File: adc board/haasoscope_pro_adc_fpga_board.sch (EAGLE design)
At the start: 562 parts, among them CN2 12Vin, IC1 ADC12DL2500ACF, IC13 LMH5401IRMST, IC14 LMH6401IRMZR, IC15 SN74AVC4T774PWR, IC17 DAC8562SDGSR, IC18 TLV9102IPWR, IC2 SN74AVC4T774PWR, IC21 LMH5401IRMST, IC22 TPS7A7200RGTR, IC23 TPS7A7200RGTR, IC24 TPS7A7200RGTR, IC25 TPS72325DBVR, IC26 TPS7A7200RGTR, IC27 TPS7A7200RGTR, IC28 TPS7A7200RGTR, IC29 LMH6401IRMZR, IC3 ADC122S021CIMM_NOPB, IC30 SN74AVC4T774PWR, IC33 TLV9102IPWR, IC4 TLV9102IPWR, IC5 EP4CE30F23C6N, IC6 EPCQ16ASI8N, IC8 FT232HQ, IC9 93LC56B, J1 2p-2.54, J10 8pin, J11 8pin, J13 8pin, J14 2x5, J15 test1, J2 test1, J30 2p-2.54, J31 2p-2.54, J32 2p-2.54, J33 2p-2.54, J34 2p-2.54, J35 2p-2.54, J36 2p-2.54, J37 2p-2.54, J39 2p-2.54, J40 2p-2.54, J41 2p-2.54, J42 2p-2.54, J43 2p-2.54, J44 2p-2.54, J45 2p-2.54, J46 2p-2.54, J8 8pin, K10 G6K-2F-RF-DC3, K11 G6K-2F-RF-DC3, K12 G6K-2F-RF-DC3, K5 AQY21SOP, K6 G6K-2F-RF-DC3, K7 G6K-2F-RF-DC3, K9 AQY21SOP, Q1 S8050, Q4 S8050, Q5 S8050, Q7 S8050, Q8 S8050, Q9 S8050, SW3 SKQGADE010, SW4 SKQGADE010, U2 ADF4350BCPZ, U6 AMS1117-1.2, X1 USBC, Y2 OSCILLATORSMD-5X3, Y3 12MHz

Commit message: make 2v5+ from 3v3 instead of 2v8+, make 1v2 from 1v5d using standard TPS7A7200RGTR instead of 3v3 with ams117-1.2
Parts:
- removed C76, C80: 10uF, Nordic_nRF:CAPACITOR_0805_N
- removed C77, C81: 0.1uF, Nordic_nRF:CAPACITOR_0402_N
- removed U6: AMS1117-1.2, MF_IC_Power:NCP1117LPST33T3G
- added C52: 10uF, Nordic_nRF:CAPACITOR_0805_N
- added C53, C54, C73: 0.1uF, Nordic_nRF:CAPACITOR_0402_N
- added IC7: TPS7A7200RGTR, TPS7A7200RGTR:TPS7A7200RGTR
- added J3: 2p-2.54, Seeed-Connector:DIP-BLACK-MALE-HEADER-VERT(2P-2.54)
- added R137: 100k, FlashPCB_Resistors:RES-0402
- added R161: 10k, FlashPCB_Resistors:RES-0402
- R230: value 56k -> 100k
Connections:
- removed net 2V8+: C278.1, C298.1, C299.1, C300.1, C301.1, IC26.EN, IC26.IN_1, IC26.IN_2, J43.1, L12.2, R229.P$2
- new net 1V5D: C278.1, C298.1, C299.1, C300.1, C301.1, C54.1, IC7.EN, IC7.IN_1, IC7.IN_2, J43.1, L12.2, R229.P$2
- new net N$23: R137.P$2, R230.P$1
- new net PG1V2: IC7.PG, R161.P$2
- net 1V2: now also C52.1, C53.1, IC7.OUT_1, IC7.OUT_2, IC7.SNS, J3.2, R161.P$1; no longer C76.2, C77.2, U6.VOUT
- net 3V3: now also C73.1, IC26.EN, IC26.IN_1, IC26.IN_2; no longer C80.2, C81.2, U6.VIN
- net GND: now also C52.2, C53.2, C54.2, C73.2, IC7.100MV, IC7.200MV, IC7.400MV, IC7.EP, IC7.GND, J3.1, R137.P$1; no longer C76.1, C77.1, C80.1, C81.1, R230.P$1, U6.GND/ADJ
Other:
- note added: "1V2 for FPGA"
- note added: "ADC power filters"
- note added: "FPGA power filters"
- note added: "For 2V5+, take input from 3V3 Only ~300mA needed"
- note added: "Rbot = Rtop/(Vout-1) =100k/(1.5-1) = 200k"
- note added: "V+ for FPGA reg ~ 1.5V"
- note removed: "Rbot = Rtop/(Vout-1) =100k/(1.5-1) = ~200k"
- note removed: "V+ for input amp reg ~ 2.8V"
- moved on the sheet: C253, C254, C275, C276, C277, C278, C298, C299, C300, C301, C34, C40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

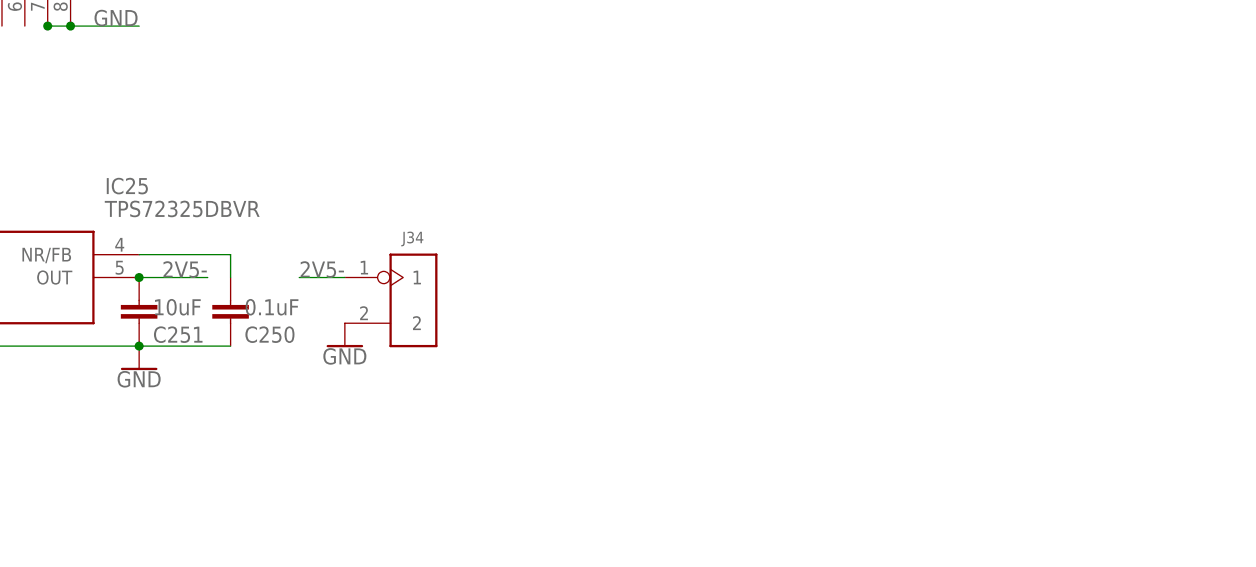
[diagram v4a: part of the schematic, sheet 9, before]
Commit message: Use 2 -2.5V regulators, one for input A, another for input B, since we need more than 200mA
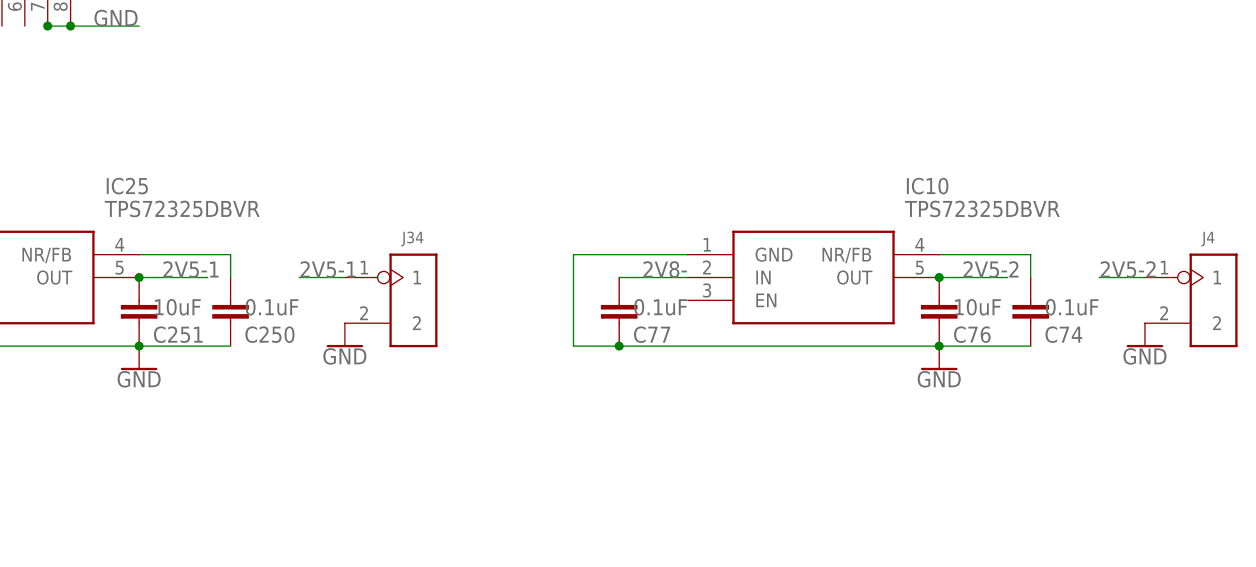
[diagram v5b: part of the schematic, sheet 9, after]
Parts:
- added C74, C77: 0.1uF, Nordic_nRF:CAPACITOR_0402_N
- added C76: 10uF, Nordic_nRF:CAPACITOR_0805_N
- added IC10: TPS72325DBVR, TPS72325DBVR:TPS72325DBVR
- added J4: 2p-2.54, Seeed-Connector:DIP-BLACK-MALE-HEADER-VERT(2P-2.54)
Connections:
- removed net 2V5-: C108.P$1, C110.P$1, C112.P$1, C129.P$1, C133.P$1, C135.P$1, C251.1, C56.P$1, C78.P$1, C85.P$1, C87.P$1, C89.P$1, C91.P$1, C95.P$1, C97.P$1, FL1.THERMAL, FL1.VS-, FL2.THERMAL, FL2.VS-, FL3.THERMAL, FL3.VS-, FL4.THERMAL, FL4.VS-, IC13.VS-_1, IC13.VS-_2, IC14.VS-_1, IC14.VS-_2, IC18.V-, IC21.VS-_1, IC21.VS-_2, IC25.OUT, IC29.VS-_1, IC29.VS-_2, IC33.V-, J34.1
- new net 2V5-1: C251.1, C78.P$1, C85.P$1, C87.P$1, C89.P$1, C91.P$1, C95.P$1, C97.P$1, FL1.THERMAL, FL1.VS-, FL3.THERMAL, FL3.VS-, IC13.VS-_1, IC13.VS-_2, IC14.VS-_1, IC14.VS-_2, IC18.V-, IC25.OUT, J34.1
- new net 2V5-2: C108.P$1, C110.P$1, C112.P$1, C129.P$1, C133.P$1, C135.P$1, C56.P$1, C76.1, FL2.THERMAL, FL2.VS-, FL4.THERMAL, FL4.VS-, IC10.OUT, IC21.VS-_1, IC21.VS-_2, IC29.VS-_1, IC29.VS-_2, IC33.V-, J4.1
- new net N$61: C74.1, IC10.NR/FB
- net 2V8-: now also C77.1, IC10.IN
- net GND: now also C74.2, C76.2, C77.2, IC10.GND, J4.2
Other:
- note added: "2A max current 180mV dropout at 2A"
- note added: "2V5- 1"
- note added: "2V5- 2"
- note added: "3A max current"
- note added: "Need separate -2v5 supplies for inputs A and B because each needs more than 100mA and each of these negative regulators can only make 200mA"
- note removed: "2V5-"
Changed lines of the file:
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@@
 <part name="GND57" library="SparkFun-PowerSymbols" library_urn="urn:adsk.eagle:library:530" deviceset="GND" device=""/>
 <part name="C73" library="Nordic_nRF" library_urn="urn:adsk.eagle:library:169009" deviceset="CAPACITOR" device="_0402_N" package3d_urn="urn:adsk.eagle:package:2593732/1" value="0.1uF"/>
+<part name="IC10" library="TPS72325DBVR" deviceset="TPS72325DBVR" device=""/>
+<part name="C74" library="Nordic_nRF" library_urn="urn:adsk.eagle:library:169009" deviceset="CAPACITOR" device="_0402_N" package3d_urn="urn:adsk.eagle:package:2593732/1" value="0.1uF"/>
+<part name="C76" library="Nordic_nRF" library_urn="urn:adsk.eagle:library:169009" deviceset="CAPACITOR" device="_0805_N" package3d_urn="urn:adsk.eagle:package:2593736/1" value="10uF"/>
+<part name="GND58" library="SparkFun-PowerSymbols" library_urn="urn:adsk.eagle:library:530" deviceset="GND" device=""/>
+<part name="C77" library="Nordic_nRF" library_urn="urn:adsk.eagle:library:169009" deviceset="CAPACITOR" device="_0402_N" package3d_urn="urn:adsk.eagle:package:2593732/1" value="0.1uF"/>
+<part name="J4" library="Seeed-Connector" library_urn="urn:adsk.eagle:library:478" deviceset="DIP-BLACK-MALE-HEADER-VERT(2P-2.54)" device="" package3d_urn="urn:adsk.eagle:package:33132/1" value="2p-2.54"/>
+<part name="GND59" library="SparkFun-PowerSymbols" library_urn="urn:adsk.eagle:library:530" deviceset="GND" device=""/>
 </parts>
 <sheets>
@@
 </segment>
 </net>
-<net name="2V5-" class="1">
+<net name="2V5-1" class="1">
 <segment>
 <wire x1="114.3" y1="238.76" x2="106.68" y2="238.76" width="0.1524" layer="91"/>
@@
 </segment>
 </net>
-<net name="2V5-" class="1">
+<net name="2V5-1" class="1">
 <segment>
 <pinref part="C85" gate="G$1" pin="P$1"/>
@@
 </segment>
 </net>
-<net name="2V5-" class="1">
+<net name="2V5-2" class="1">
 <segment>
 <wire x1="86.36" y1="198.12" x2="78.74" y2="198.12" width="0.1524" layer="91"/>
@@
 </segment>
 </net>
-<net name="2V5-" class="1">
+<net name="2V5-2" class="1">
 <segment>
 <pinref part="C108" gate="G$1" pin="P$1"/>
@@
 <text x="233.68" y="264.16" size="1.778" layer="90">VFPGA25 = 2.5V</text>
 <text x="231.14" y="180.34" size="1.778" layer="90">2V5+</text>
-<text x="246.38" y="124.46" size="1.778" layer="90">2V5-</text>
+<text x="246.38" y="124.46" size="1.778" layer="90">2V5- 1</text>
 <text x="279.4" y="236.22" size="1.778" layer="90">= 0.5 + grounded inputs</text>
 <text x="180.34" y="378.46" size="1.778" layer="90">Rbot = Rtop/(Vout-1)
@@
 <text x="205.74" y="-20.32" size="1.778" layer="90">1V2
 for FPGA</text>
+<text x="327.66" y="464.82" size="1.778" layer="90">2A max current
+180mV dropout at 2A</text>
+<text x="119.38" y="487.68" size="1.778" layer="90">3A max current</text>
+<text x="335.28" y="124.46" size="1.778" layer="90">2V5- 2</text>
+<text x="266.7" y="96.52" size="1.778" layer="90">Need separate -2v5 supplies for inputs A and B because each needs more than 100mA
+and each of these negative regulators can only make 200mA</text>
 </plain>
 <instances>
@@
 <attribute name="VALUE" x="291.084" y="163.449" size="1.778" layer="96"/>
 </instance>
+<instance part="IC10" gate="G$1" x="332.74" y="119.38" smashed="yes">
+<attribute name="NAME" x="356.87" y="127" size="1.778" layer="95" align="center-left"/>
+<attribute name="VALUE" x="356.87" y="124.46" size="1.778" layer="96" align="center-left"/>
+</instance>
+<instance part="C74" gate="C$1" x="370.84" y="114.3" smashed="yes">
+<attribute name="NAME" x="372.364" y="109.601" size="1.778" layer="95"/>
+<attribute name="VALUE" x="372.364" y="112.649" size="1.778" layer="96"/>
+</instance>
+<instance part="C76" gate="C$1" x="360.68" y="114.3" smashed="yes">
+<attribute name="NAME" x="362.204" y="109.601" size="1.778" layer="95"/>
+<attribute name="VALUE" x="362.204" y="112.649" size="1.778" layer="96"/>
+</instance>
+<instance part="GND58" gate="1" x="360.68" y="106.68" smashed="yes">
+<attribute name="VALUE" x="360.68" y="106.426" size="1.778" layer="96" align="top-center"/>
+</instance>
+<instance part="C77" gate="C$1" x="325.12" y="114.3" smashed="yes">
+<attribute name="NAME" x="326.644" y="109.601" size="1.778" layer="95"/>
+<attribute name="VALUE" x="326.644" y="112.649" size="1.778" layer="96"/>
+</instance>
+<instance part="J4" gate="G$1" x="391.16" y="114.3" smashed="yes">
+<attribute name="NAME" x="389.89" y="120.65" size="1.27" layer="95" ratio="10"/>
+</instance>
+<instance part="GND59" gate="1" x="383.54" y="109.22" smashed="yes">
+<attribute name="VALUE" x="383.54" y="108.966" size="1.778" layer="96" align="top-center"/>
+</instance>
 </instances>
 <busses>
@@
 <label x="215.9" y="127" size="1.778" layer="95"/>
 </segment>
+<segment>
+<wire x1="332.74" y1="116.84" x2="325.12" y2="116.84" width="0.1524" layer="91"/>
+<label x="327.66" y="116.84" size="1.778" layer="95"/>
+<pinref part="IC10" gate="G$1" pin="IN"/>
+<pinref part="C77" gate="C$1" pin="1"/>
+</segment>
 </net>
 <net name="GND" class="4">
@@
 <pinref part="GND57" gate="1" pin="GND"/>
 </segment>
+<segment>
+<wire x1="370.84" y1="109.22" x2="360.68" y2="109.22" width="0.1524" layer="91"/>
+<junction x="360.68" y="109.22"/>
+<wire x1="325.12" y1="109.22" x2="320.04" y2="109.22" width="0.1524" layer="91"/>
+<junction x="325.12" y="109.22"/>
+<wire x1="320.04" y1="109.22" x2="320.04" y2="119.38" width="0.1524" layer="91"/>
+<wire x1="332.74" y1="119.38" x2="320.04" y2="119.38" width="0.1524" layer="91"/>
+<wire x1="360.68" y1="109.22" x2="325.12" y2="109.22" width="0.1524" layer="91"/>
+<pinref part="IC10" gate="G$1" pin="GND"/>
+<pinref part="C74" gate="C$1" pin="2"/>
+<pinref part="C76" gate="C$1" pin="2"/>
+<pinref part="GND58" gate="1" pin="GND"/>
+<pinref part="C77" gate="C$1" pin="2"/>
+</segment>
+<segment>
+<pinref part="GND59" gate="1" pin="GND"/>
+<pinref part="J4" gate="G$1" pin="2"/>
+</segment>
 </net>
 <net name="N$101" class="0">
@@
 </segment>
 </net>
-<net name="2V5-" class="1">
+<net name="2V5-1" class="1">
 <segment>
 <pinref part="IC25" gate="G$1" pin="OUT"/>
@@
 </segment>
 </net>
+<net name="N$61" class="0">
+<segment>
+<wire x1="360.68" y1="119.38" x2="370.84" y2="119.38" width="0.1524" layer="91"/>
+<wire x1="370.84" y1="119.38" x2="370.84" y2="116.84" width="0.1524" layer="91"/>
+<pinref part="IC10" gate="G$1" pin="NR/FB"/>
+<pinref part="C74" gate="C$1" pin="1"/>
+</segment>
+</net>
+<net name="2V5-2" class="1">
+<segment>
+<wire x1="360.68" y1="116.84" x2="368.3" y2="116.84" width="0.1524" layer="91"/>
+<junction x="360.68" y="116.84"/>
+<label x="363.22" y="116.84" size="1.778" layer="95"/>
+<pinref part="IC10" gate="G$1" pin="OUT"/>
+<pinref part="C76" gate="C$1" pin="1"/>
+</segment>
+<segment>
+<wire x1="383.54" y1="116.84" x2="378.46" y2="116.84" width="0.1524" layer="91"/>
+<label x="378.46" y="116.84" size="1.778" layer="95"/>
+<pinref part="J4" gate="G$1" pin="1"/>
+</segment>
+</net>

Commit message: change -2v8 to -3v0 for more dropout headroom on -2v5 regulator
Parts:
- added R209: 100k, FlashPCB_Resistors:RES-0402
- R232: value 56k -> 100k
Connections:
- removed net 2V8-: C252.1, C279.2, C281.2, C282.2, C288.2, C294.2, C295.2, C296.2, C297.2, C77.1, D10.A, IC10.IN, IC25.IN, J44.2, PS13.EP, PS13.PGND, R232.P$1
- new net 3V0-: C252.1, C279.2, C281.2, C282.2, C288.2, C294.2, C295.2, C296.2, C297.2, C77.1, D10.A, IC10.IN, IC25.IN, J44.2, PS13.EP, PS13.PGND, R209.P$1, R232.P$1
- net N$127: now also R209.P$2
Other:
- note added: "Rbot = Rtop/(Vout-1) =100k/(3.0-1) = 50k"
- note added: "V- for input amp reg ~ -3.0V"
- note removed: "V- for input amp reg ~ -2.8V"
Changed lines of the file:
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@@
 <part name="J44" library="Seeed-Connector" library_urn="urn:adsk.eagle:library:478" deviceset="DIP-BLACK-MALE-HEADER-VERT(2P-2.54)" device="" package3d_urn="urn:adsk.eagle:package:33132/1" value="2p-2.54"/>
 <part name="R231" library="FlashPCB_Resistors" deviceset="RES-0402" device="" value="100k"/>
-<part name="R232" library="FlashPCB_Resistors" deviceset="RES-0402" device="" value="56k"/>
+<part name="R232" library="FlashPCB_Resistors" deviceset="RES-0402" device="" value="100k"/>
 <part name="PS14" library="LMR33630ADDA" deviceset="LMR33630ADDA" device="">
 <attribute name="LCSC" value="C841384"/>
@@
 <part name="J4" library="Seeed-Connector" library_urn="urn:adsk.eagle:library:478" deviceset="DIP-BLACK-MALE-HEADER-VERT(2P-2.54)" device="" package3d_urn="urn:adsk.eagle:package:33132/1" value="2p-2.54"/>
 <part name="GND59" library="SparkFun-PowerSymbols" library_urn="urn:adsk.eagle:library:530" deviceset="GND" device=""/>
+<part name="R209" library="FlashPCB_Resistors" deviceset="RES-0402" device="" value="100k"/>
+<part name="GND60" library="SparkFun-PowerSymbols" library_urn="urn:adsk.eagle:library:530" deviceset="GND" device=""/>
 </parts>
 <sheets>
@@
 =100k/(3.7-1) = ~37k</text>
 <text x="71.12" y="-5.08" size="1.778" layer="90">V+ for FPGA reg ~ 1.5V</text>
-<text x="124.46" y="124.46" size="1.778" layer="90">V- for input amp reg ~ -2.8V</text>
+<text x="124.46" y="124.46" size="1.778" layer="90">V- for input amp reg ~ -3.0V</text>
 <text x="121.92" y="335.28" size="1.778" layer="90">V for 1.9V reg ~ 2.2V</text>
 <text x="119.38" y="406.4" size="1.778" layer="90">V for 1.1V reg ~ 1.5V</text>
@@
 <text x="132.08" y="-33.02" size="1.778" layer="90">Rbot = Rtop/(Vout-1)
 =100k/(1.5-1) = 200k</text>
-<text x="182.88" y="96.52" size="1.778" layer="90">Rbot = Rtop/(Vout-1)
-=100k/(2.8-1) = ~55k</text>
+<text x="190.5" y="96.52" size="1.778" layer="90">Rbot = Rtop/(Vout-1)
+=100k/(3.0-1) = 50k</text>
 <text x="210.82" y="76.2" size="1.778" layer="90">Make 5V from 12V in case USB C insufficient</text>
 <wire x1="5.08" y1="297.18" x2="381" y2="297.18" width="0.1524" layer="97"/>
@@
 <attribute name="VALUE" x="383.54" y="108.966" size="1.778" layer="96" align="top-center"/>
 </instance>
+<instance part="R209" gate="G$1" x="182.88" y="99.06" smashed="yes" rot="R90">
+<attribute name="NAME" x="181.3814" y="95.25" size="1.778" layer="95" rot="R90"/>
+<attribute name="VALUE" x="186.182" y="95.25" size="1.778" layer="96" rot="R90"/>
+</instance>
+<instance part="GND60" gate="1" x="289.56" y="160.02" smashed="yes">
+<attribute name="VALUE" x="289.56" y="159.766" size="1.778" layer="96" align="top-center"/>
+</instance>
 </instances>
 <busses>
 </busses>
 <nets>
-<net name="2V8-" class="0">
+<net name="3V0-" class="0">
 <segment>
 <pinref part="IC25" gate="G$1" pin="IN"/>
@@
 <wire x1="114.3" y1="91.44" x2="134.62" y2="91.44" width="0.1524" layer="91"/>
 <junction x="134.62" y="91.44"/>
+<pinref part="R209" gate="G$1" pin="P$1"/>
+<wire x1="182.88" y1="93.98" x2="175.26" y2="93.98" width="0.1524" layer="91"/>
+<junction x="175.26" y="93.98"/>
 </segment>
 <segment>
@@
 <segment>
 <pinref part="IC26" gate="G$1" pin="1.6V"/>
-<wire x1="276.86" y1="165.1" x2="287.02" y2="165.1" width="0.1524" layer="91"/>
+<wire x1="276.86" y1="165.1" x2="284.48" y2="165.1" width="0.1524" layer="91"/>
 <label x="279.4" y="165.1" size="1.778" layer="95"/>
-<pinref part="C73" gate="C$1" pin="2"/>
-<wire x1="287.02" y1="165.1" x2="287.02" y2="162.56" width="0.1524" layer="91"/>
-<wire x1="287.02" y1="162.56" x2="289.56" y2="162.56" width="0.1524" layer="91"/>
 </segment>
 <segment>
@@
 <pinref part="J4" gate="G$1" pin="2"/>
 </segment>
+<segment>
+<pinref part="C73" gate="C$1" pin="2"/>
+<pinref part="GND60" gate="1" pin="GND"/>
+</segment>
 </net>
 <net name="N$101" class="0">
@@
 <wire x1="149.86" y1="104.14" x2="175.26" y2="104.14" width="0.1524" layer="91"/>
 <junction x="175.26" y="104.14"/>
+<pinref part="R209" gate="G$1" pin="P$2"/>
+<wire x1="182.88" y1="104.14" x2="175.26" y2="104.14" width="0.1524" layer="91"/>
 </segment>
 </net>

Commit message: minor
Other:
- note added: "Slow adc for temp monitoring"
- note removed: "Slow adc for temp momitoring"
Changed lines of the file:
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@@
 <description>Temp mon</description>
 <plain>
-<text x="22.86" y="17.78" size="1.778" layer="90">Slow adc for temp momitoring</text>
+<text x="22.86" y="17.78" size="1.778" layer="90">Slow adc for temp monitoring</text>
 <text x="99.06" y="101.6" size="1.778" layer="90">V across TDIODE, with 0.1mA
 is 0.681 when ADC running with clock, 0.731 when off</text>

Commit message: use cutouts under 3GHz relays
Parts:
- removed K10, K11, K12: G6K-2F-RF-DC3, G6K-2F-RF-DC3:G6K-2F-RF-DC3
- removed K9: AQY21SOP, relay:AQY21SOP
- removed R136, R160: 1k, MF_Passives:RESISTOR_0402
- added K1, K2, K3, K4: G6K-2F-RF-T-TR03_DC5, G6K-2F-RF-T-TR03_DC5:G6K-2F-RF-T-TR03_DC5
- K5: value AQY21SOP -> G6K-2F-RF-T-TR03_DC5; device relay:AQY21SOP -> G6K-2F-RF-T-TR03_DC5:G6K-2F-RF-T-TR03_DC5; LCSC C7435105 -> (none); MPN AQY210S -> (none)
- K6, K7: value G6K-2F-RF-DC3 -> TLP3475R_TP,F; device G6K-2F-RF-DC3:G6K-2F-RF-DC3 -> TLP3475R_TP_F:TLP3475R_TP,F; LCSC C397195 -> (none); MANUFACTURER_PART_NUMBER (none) -> TLP3475R(TP,F
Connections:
- net 10KHZOUT renamed 1KHZOUT
- removed net N$13: K5.A, R136.P$1
- removed net N$52: K9.A, R160.P$1
- removed net OUTMAIN: K12.COM_2, R134.P$1, R135.P$2
- removed net OUTPATHACDC: C82.P$2, K12.COM_1, K9.DS1
- removed net OUTPATHACDC2: C72.P$2, K5.DS1, R192.P$1, R193.P$2
- new net OUTPATHMAIN: C82.P$2, K7.DRAIN_2, R134.P$1, R135.P$2
- new net OUTPATHMAIN2: C72.P$2, K6.DRAIN_2, R192.P$1, R193.P$2
- new net OUTSPLITTER: K1.COM_2, K2.COM_1
- net 1MPATH: now also K2.NO_1; no longer K10.NO_1
- net 1MPATH2: now also K4.NO_1; no longer K6.NO_1
- net 1MPATH50: now also K2.NO_2; no longer K10.NO_2
- net 1MPATH502: now also K4.NO_2; no longer K6.NO_2
- net 50PATH: now also K2.NC_1, K2.NC_2; no longer K10.NC_1, K10.NC_2
- net 50PATH2: now also K4.NC_1, K4.NC_2; no longer K6.NC_1, K6.NC_2
- net 5V: now also K1.COIL+, K2.COIL+, K3.COIL+, K4.COIL+, K5.COIL+; no longer K10.COIL+, K11.COIL+, K12.COIL+, K6.COIL+, K7.COIL+
- net ACDC_CONTROL: now also K7.ANODE; no longer R160.P$2
- net ACDC_CONTROL2: now also K6.ANODE; no longer R136.P$2
- net COIL1-: now also K2.COIL-; no longer K10.COIL-
- net COIL1-2: now also K4.COIL-; no longer K6.COIL-
- net COIL2-: now also K3.COIL-; no longer K11.COIL-
- net COIL2-2: now also K5.COIL-; no longer K7.COIL-
- net COIL3-: now also K1.COIL-; no longer K12.COIL-
- net FILTIN: now also K3.NO_1; no longer K11.NO_1
- net FILTIN2: now also K5.NO_1; no longer K7.NO_1
- net FILTOUT: now also K3.NO_2; no longer K11.NO_2
- net FILTOUT2: now also K5.NO_2; no longer K7.NO_2
- net GND: now also K1.GND_1, K1.GND_10, K1.GND_2, K1.GND_3, K1.GND_4, K1.GND_5, K1.GND_6, K1.GND_7, K1.GND_8, K1.GND_9, K2.GND_1, K2.GND_10, K2.GND_2, K2.GND_3, K2.GND_4, K2.GND_5, K2.GND_6, K2.GND_7, K2.GND_8, K2.GND_9, K3.GND_1, K3.GND_10, K3.GND_2, K3.GND_3, K3.GND_4, K3.GND_5, K3.GND_6, K3.GND_7, K3.GND_8, K3.GND_9, K4.GND_1, K4.GND_10, K4.GND_2, K4.GND_3, K4.GND_4, K4.GND_5, K4.GND_6, K4.GND_7, K4.GND_8, K4.GND_9, K5.GND_1, K5.GND_10, K5.GND_2, K5.GND_3, K5.GND_4, K5.GND_5, K5.GND_6, K5.GND_7, K5.GND_8, K5.GND_9, K6.CATHODE, K7.CATHODE; no longer K10.MP1, K10.MP2, K11.MP1, K11.MP2, K12.MP1, K12.MP2, K5.K, K6.MP1, K6.MP2, K7.MP1, K7.MP2, K9.K
- net INPATH: now also K1.COM_1; no longer K10.COM_1
- net INPATH2: now also K4.COM_1; no longer K6.COM_1
- net NOFILT: now also K3.NC_1, K3.NC_2; no longer K11.NC_1, K11.NC_2
- net NOFILT2: now also K5.NC_1, K5.NC_2; no longer K7.NC_1, K7.NC_2
- net NOSPLIT: now also K1.NC_1, K1.NC_2; no longer K12.NC_1, K12.NC_2
- net OUTPATH: now also K2.COM_2, K3.COM_1; no longer K10.COM_2, K11.COM_1
- net OUTPATH2: now also K4.COM_2, K5.COM_1; no longer K6.COM_2, K7.COM_1
- net OUTPATHFILT: now also K3.COM_2, K7.DRAIN_1; no longer K11.COM_2, K9.DS2
- net OUTPATHFILT2: now also K5.COM_2, K6.DRAIN_1; no longer K5.DS2, K7.COM_2
- net SPLIT: now also K1.NO_1; no longer K12.NO_1
- net SPLITOUT: now also K1.NO_2; no longer K12.NO_2
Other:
- note added: "5V USB for front panel"
- note added: "BNC input"
- moved on the sheet: BNCIN2, J15, OUTSPLIT, Q9, R168, R169, R170, R171
